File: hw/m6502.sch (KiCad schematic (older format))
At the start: 15 parts, among them SW1 SW_Push, U1 MAX708, U2 XTAL_OSC, U3 6502, U4 74HCT00, U5 74HCT138, U6 HM62256BLP-7, U7 28C256

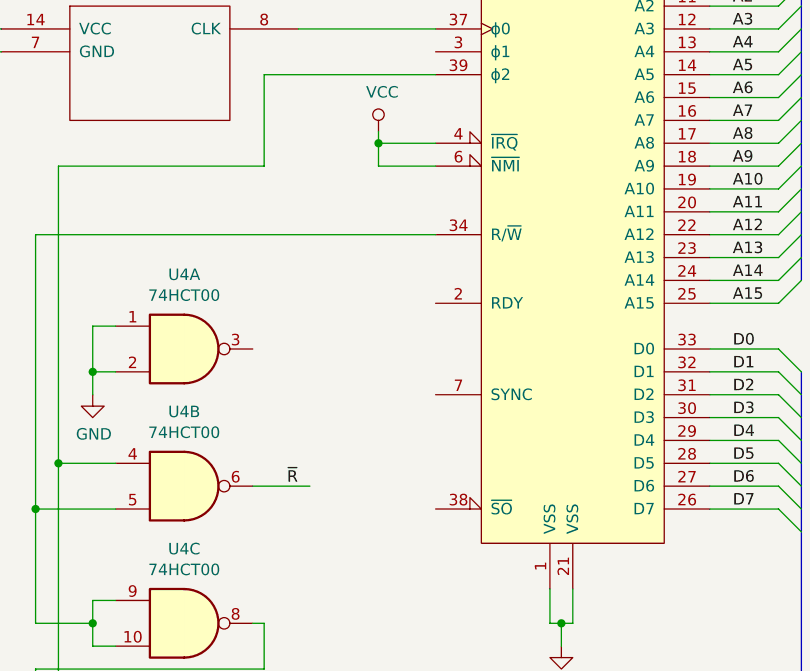
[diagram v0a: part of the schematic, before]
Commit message: tie RDY and -SO high
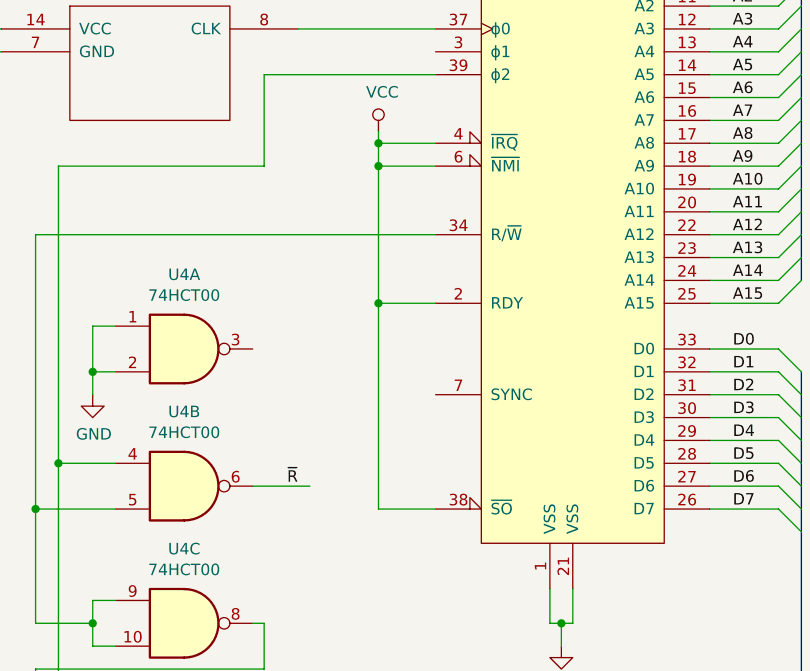
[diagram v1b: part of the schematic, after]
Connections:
- wire segments 188 -> 192
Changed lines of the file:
@@
 EESchema Schematic File Version 4
+LIBS:m6502-cache
 EELAYER 26 0
 EELAYER END
@@
 Wire Wire Line
 	3150 7300 3150 7400
+Connection ~ 3150 7400
+Wire Wire Line
+	3150 7400 2800 7400
+$Comp
+L power:VCC #PWR?
+U 1 1 5D913677
+P 2800 6800
+F 0 "#PWR?" H 2800 6650 50  0001 C CNN
+F 1 "VCC" H 2817 6973 50  0000 C CNN
+F 2 "" H 2800 6800 50  0001 C CNN
+F 3 "" H 2800 6800 50  0001 C CNN
+	1    2800 6800
+	1    0    0    -1
+$EndComp
+$Comp
+L power:GND #PWR?
+U 1 1 5D9136FE
+P 2800 7500
+F 0 "#PWR?" H 2800 7250 50  0001 C CNN
+F 1 "GND" H 2805 7327 50  0000 C CNN
+F 2 "" H 2800 7500 50  0001 C CNN
+F 3 "" H 2800 7500 50  0001 C CNN
+	1    2800 7500
+	1    0    0    -1
+$EndComp
+Text Notes 1850 7850 0    50   ~ 0
+Decoupling caps: place near power pins of U3-U7
+Wire Wire Line
+	3350 3900 3100 3900
+Wire Wire Line
+	3100 3900 3100 3300
+Connection ~ 3100 3300
+Wire Wire Line
+	3350 4800 3100 4800
+Wire Wire Line
+	3100 4800 3100 3900
 Wire Bus Line
 	5050 600  7950 600
@@
 Wire Bus Line
 	8050 700  8050 4900
-Connection ~ 3150 7400
-Wire Wire Line
-	3150 7400 2800 7400
-$Comp
-L power:VCC #PWR?
-U 1 1 5D913677
-P 2800 6800
-F 0 "#PWR?" H 2800 6650 50  0001 C CNN
-F 1 "VCC" H 2817 6973 50  0000 C CNN
-F 2 "" H 2800 6800 50  0001 C CNN
-F 3 "" H 2800 6800 50  0001 C CNN
-	1    2800 6800
-	1    0    0    -1
-$EndComp
-$Comp
-L power:GND #PWR?
-U 1 1 5D9136FE
-P 2800 7500
-F 0 "#PWR?" H 2800 7250 50  0001 C CNN
-F 1 "GND" H 2805 7327 50  0000 C CNN
-F 2 "" H 2800 7500 50  0001 C CNN
-F 3 "" H 2800 7500 50  0001 C CNN
-	1    2800 7500
-	1    0    0    -1
-$EndComp
-Text Notes 1850 7850 0    50   ~ 0
-Decoupling caps: place near power pins of U3-U7
+Connection ~ 3100 3900
 $EndSCHEMATC
